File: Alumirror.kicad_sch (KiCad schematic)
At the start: 42 parts, among them J1 USB_C_Receptacle_USB2.0_16P_2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, J2 USB_C_Receptacle_USB2.0_16P_2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, J3 USB_C_Receptacle_USB2.0_16P_2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, J4 USB_C_Receptacle_USB2.0_16P_2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, SW10 BOOT, U1 CH552T, U2 CH552T, U3 USBLC6-2P6, U4 USBLC6-2P6, U5 USBLC6-2P6, U6 USBLC6-2P6

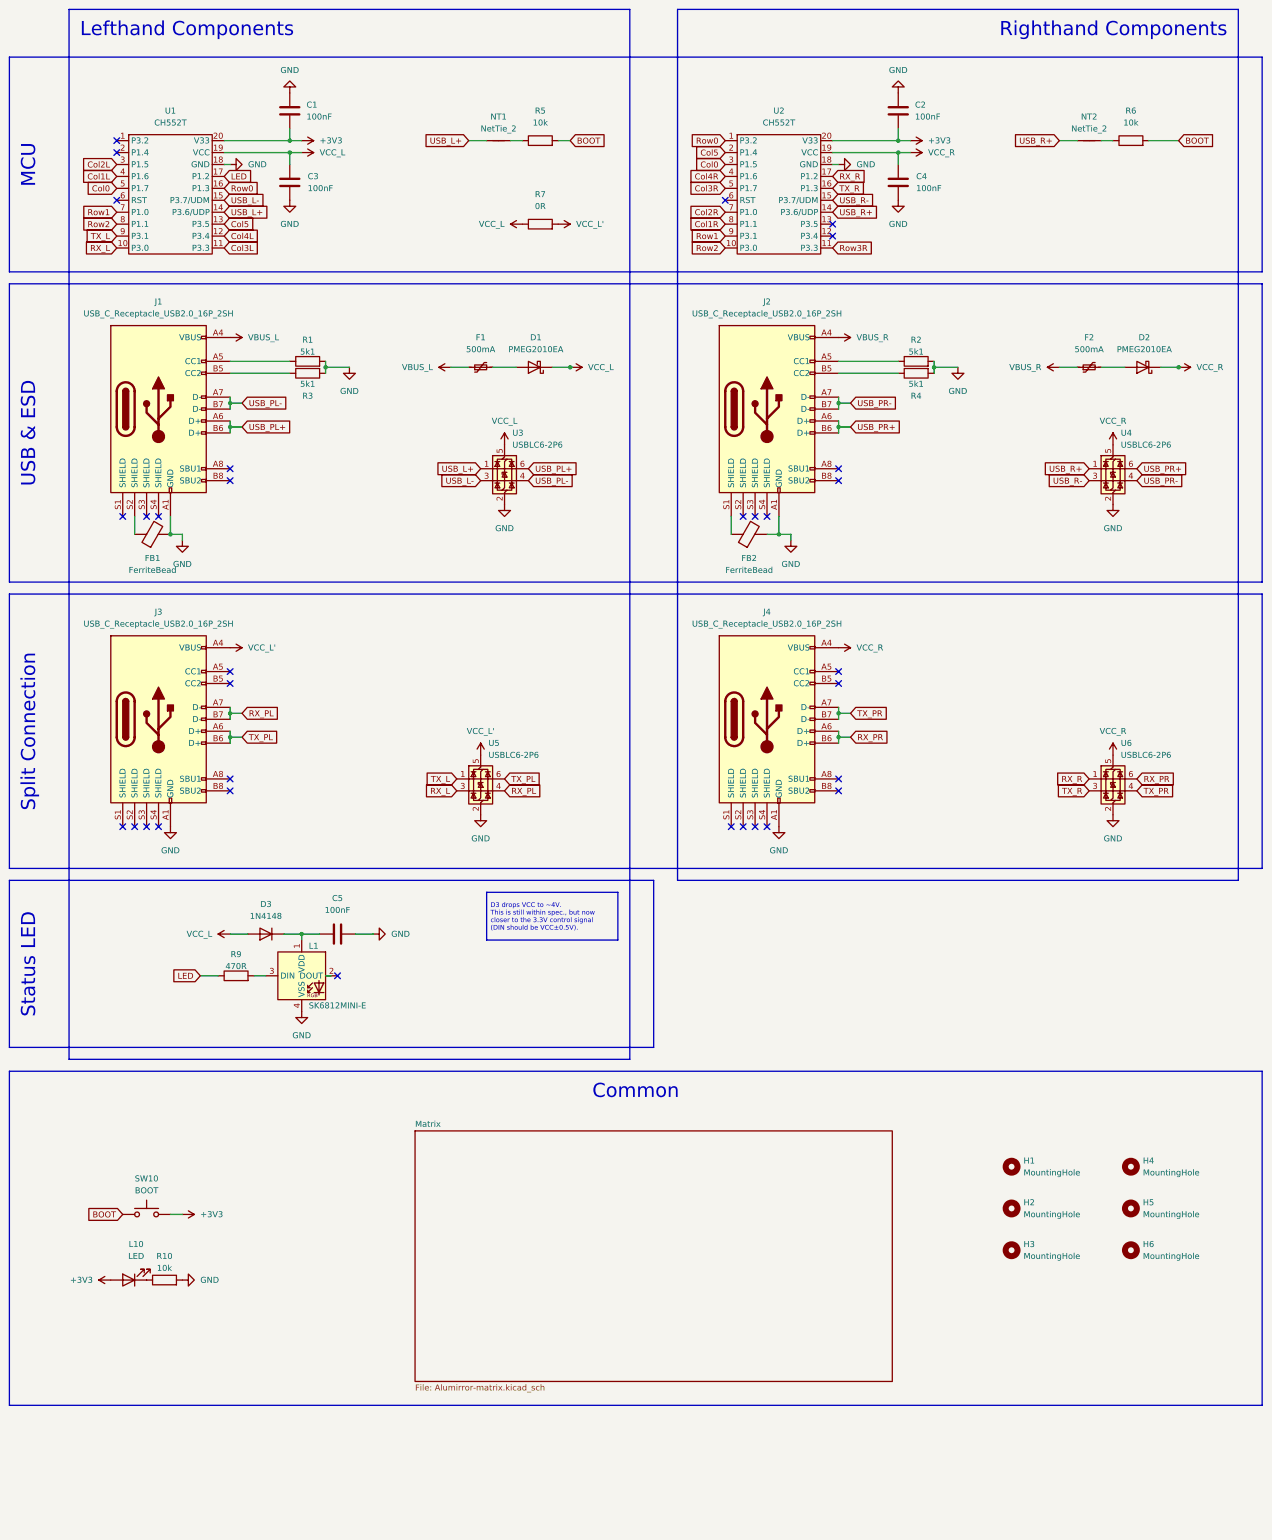
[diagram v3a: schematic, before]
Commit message: Renumber matrix switches and diodes
Columns and rows start from 1 rather than 0.
All components now follow the rules from the previous change, and we don’t had to mess around with the fake D-“oh” nonsense.
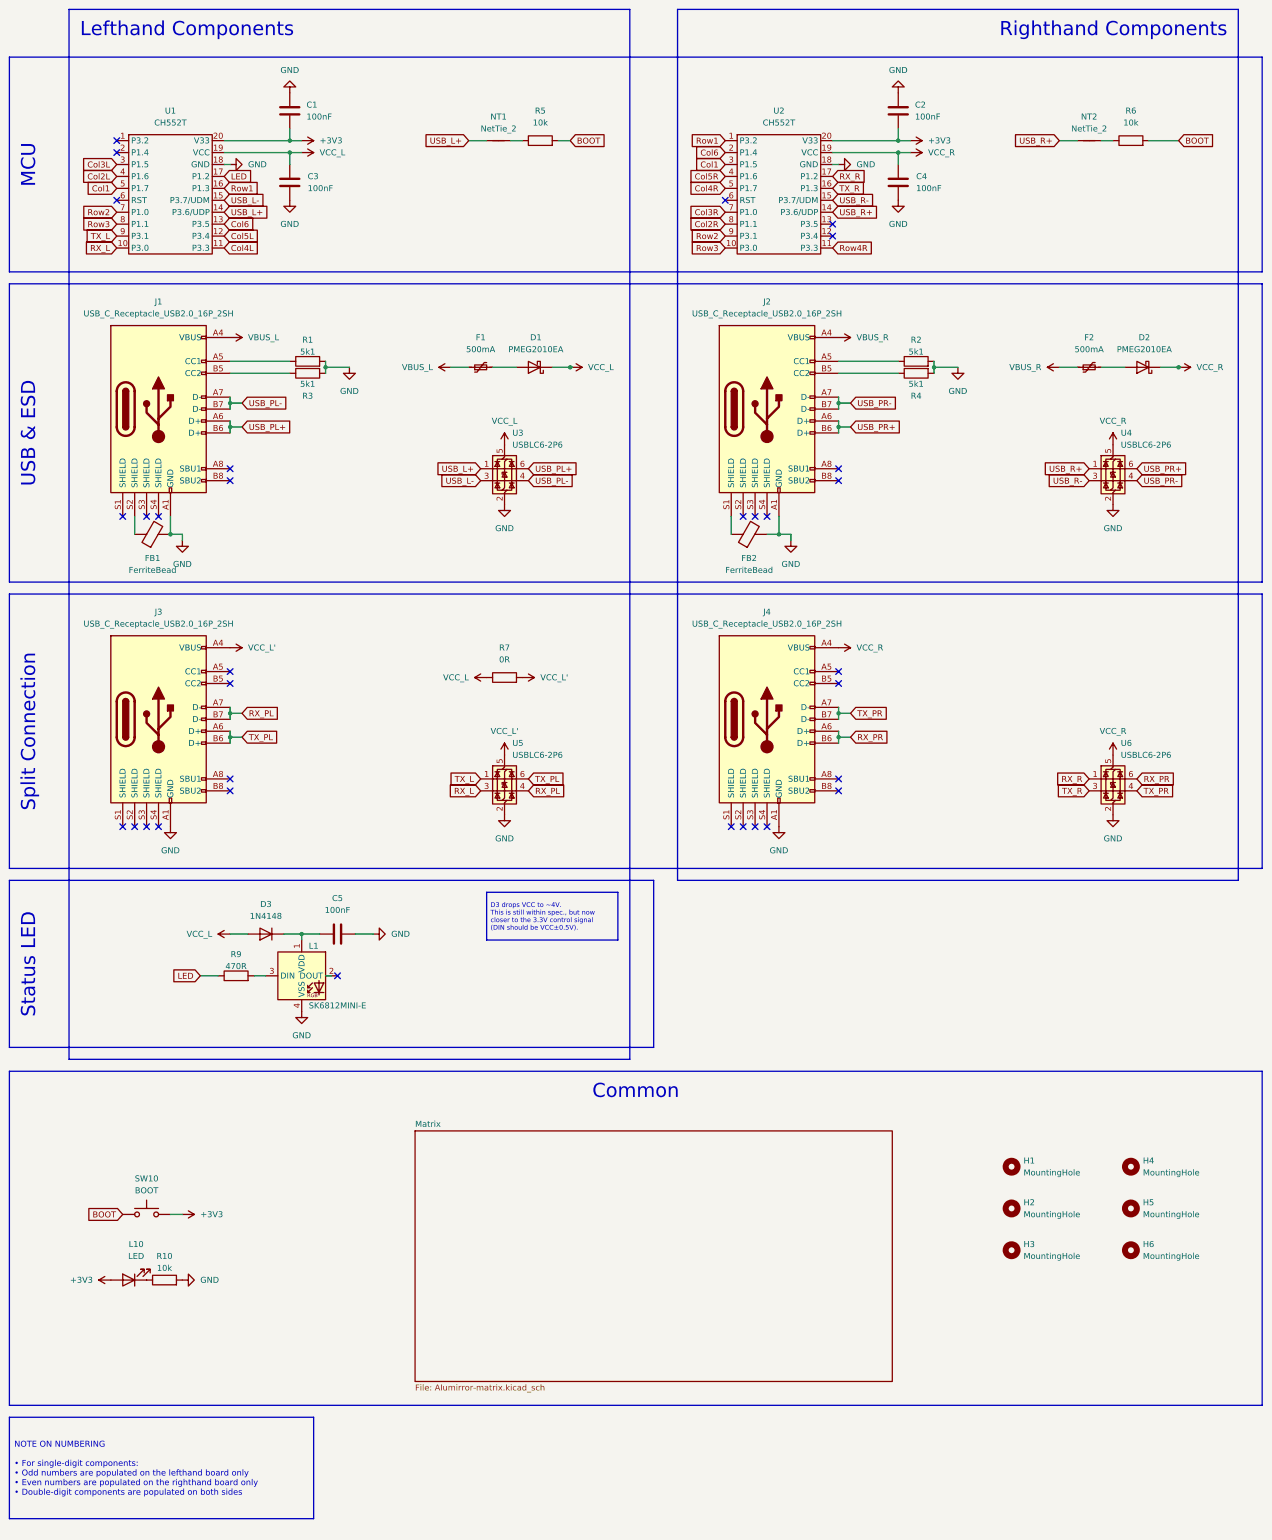
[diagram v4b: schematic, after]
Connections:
- net Col1L is gone; now on net Col2L: U1.4 (P1.6)
- net Col1R is gone; now on net Col2R: U2.8 (P1.1)
- net Row0 is gone; now on net Row1: U1.16 (P1.3), U2.1 (P3.2)
- net Col2L: no longer U1.3 (P1.5)
- net Col2R: no longer U2.7 (P1.0)
- net Col3L: now also U1.3 (P1.5); no longer U1.11 (P3.3)
- net Col3R: now also U2.7 (P1.0); no longer U2.5 (P1.7)
- net Col4L: now also U1.11 (P3.3); no longer U1.12 (P3.4)
- net Col4R: now also U2.5 (P1.7); no longer U2.4 (P1.6)
- net Row1: no longer U1.7 (P1.0), U2.9 (P3.1)
- net Row2: now also U1.7 (P1.0), U2.9 (P3.1); no longer U1.8 (P1.1), U2.10 (P3.0)
- net Col0 renamed Col1
- net Col5 renamed Col6
- net Row3R renamed Row4R
- new net Col5L: U1.12 (P3.4)
- new net Col5R: U2.4 (P1.6)
- new net Row3: U1.8 (P1.1), U2.10 (P3.0)
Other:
- moved on the sheet: R7, U5
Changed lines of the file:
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@@
 		)
 	)
+	(text_box "NOTE ON NUMBERING\n\n• For single-digit components:\n  • Odd numbers are populated on the lefthand board only\n  • Even numbers are populated on the righthand board only\n• Double-digit components are populated on both sides"
+		(exclude_from_sim no)
+		(at 15.24 314.96 0)
+		(size 64.77 21.59)
+		(stroke
+			(width 0)
+			(type default)
+		)
+		(fill
+			(type none)
+		)
+		(effects
+			(font
+				(size 1.27 1.27)
+			)
+			(justify left)
+		)
+	)
 	(text_box "Split Connection"
 		(exclude_from_sim no)
@@
 		)
 	)
-	(global_label "Col0"
+	(global_label "Col1"
 		(shape input)
 		(at 38.1 53.34 180)
@@
 	(global_label "TX_PL"
 		(shape input)
-		(at 120.65 179.07 0)
+		(at 125.73 179.07 0)
 		(fields_autoplaced yes)
 		(effects
@@
 		)
 		(property "Intersheetrefs" "${INTERSHEET_REFS}"
-			(at 129.078 179.07 0)
+			(at 134.158 179.07 0)
 			(effects
 				(font
@@
 		)
 	)
-	(global_label "Col4L"
+	(global_label "Col5L"
 		(shape input)
 		(at 60.96 63.5 0)
@@
 		)
 	)
-	(global_label "Row2"
+	(global_label "Row3"
 		(shape input)
 		(at 38.1 60.96 180)
@@
 		)
 	)
-	(global_label "Row1"
+	(global_label "Row2"
 		(shape input)
 		(at 38.1 58.42 180)
@@
 		)
 	)
-	(global_label "Col2L"
+	(global_label "Col3L"
 		(shape input)
 		(at 38.1 48.26 180)
@@
 		)
 	)
-	(global_label "Col1L"
+	(global_label "Col2L"
 		(shape input)
 		(at 38.1 50.8 180)
@@
 		)
 	)
-	(global_label "Col4R"
+	(global_label "Col5R"
 		(shape input)
 		(at 167.64 50.8 180)
@@
 		)
 	)
-	(global_label "Col3R"
+	(global_label "Col4R"
 		(shape input)
 		(at 167.64 53.34 180)
@@
 		)
 	)
-	(global_label "Col3L"
+	(global_label "Col4L"
 		(shape input)
 		(at 60.96 66.04 0)
@@
 		)
 	)
-	(global_label "Row3R"
+	(global_label "Row4R"
 		(shape input)
 		(at 190.5 66.04 0)
@@
 	(global_label "RX_L"
 		(shape input)
-		(at 110.49 181.61 180)
+		(at 115.57 181.61 180)
 		(fields_autoplaced yes)
 		(effects
@@
 		)
 		(property "Intersheetrefs" "${INTERSHEET_REFS}"
-			(at 103.0296 181.61 0)
+			(at 108.1096 181.61 0)
 			(effects
 				(font
@@
 		)
 	)
-	(global_label "Col1R"
+	(global_label "Col2R"
 		(shape input)
 		(at 167.64 60.96 180)
@@
 		)
 	)
-	(global_label "Row1"
+	(global_label "Row2"
 		(shape input)
 		(at 167.64 63.5 180)
@@
 	(global_label "TX_L"
 		(shape input)
-		(at 110.49 179.07 180)
+		(at 115.57 179.07 180)
 		(fields_autoplaced yes)
 		(effects
@@
 		)
 		(property "Intersheetrefs" "${INTERSHEET_REFS}"
-			(at 103.332 179.07 0)
+			(at 108.412 179.07 0)
 			(effects
 				(font
@@
 		)
 	)
-	(global_label "Col5"
+	(global_label "Col6"
 		(shape input)
 		(at 60.96 60.96 0)
@@
 		)
 	)
-	(global_label "Row2"
+	(global_label "Row3"
 		(shape input)
 		(at 167.64 66.04 180)
@@
 		)
 	)
-	(global_label "Col0"
+	(global_label "Col1"
 		(shape input)
 		(at 167.64 48.26 180)
@@
 		)
 	)
-	(global_label "Row0"
+	(global_label "Row1"
 		(shape input)
 		(at 60.96 53.34 0)
@@
 		)
 	)
-	(global_label "Row0"
+	(global_label "Row1"
 		(shape input)
 		(at 167.64 43.18 180)
@@
 		)
 	)
-	(global_label "Col5"
+	(global_label "Col6"
 		(shape input)
 		(at 167.64 45.72 180)
@@
 	(global_label "RX_PL"
 		(shape input)
-		(at 120.65 181.61 0)
+		(at 125.73 181.61 0)
 		(fields_autoplaced yes)
 		(effects
@@
 		)
 		(property "Intersheetrefs" "${INTERSHEET_REFS}"
-			(at 129.3804 181.61 0)
+			(at 134.4604 181.61 0)
 			(effects
 				(font
@@
 		)
 	)
-	(global_label "Col2R"
+	(global_label "Col3R"
 		(shape input)
 		(at 167.64 58.42 180)
@@
 	(symbol
 		(lib_id "power:VCC")
-		(at 115.57 173.99 0)
+		(at 120.65 173.99 0)
 		(unit 1)
 		(exclude_from_sim no)
@@
 		(fields_autoplaced yes)
 		(property "Reference" "#PWR02"
-			(at 115.57 177.8 0)
+			(at 120.65 177.8 0)
 			(effects
 				(font
@@
 		)
 		(property "Value" "VCC_L'"
-			(at 115.57 168.91 0)
+			(at 120.65 168.91 0)
 			(effects
 				(font
@@
 		)
 		(property "Footprint" ""
-			(at 115.57 173.99 0)
+			(at 120.65 173.99 0)
 			(effects
 				(font
@@
 		)
 		(property "Datasheet" ""
-			(at 115.57 173.99 0)
+			(at 120.65 173.99 0)
 			(effects
 				(font
@@
 		)
 		(property "Description" ""
-			(at 115.57 173.99 0)
+			(at 120.65 173.99 0)
 			(effects
 				(font
@@
 	(symbol
 		(lib_id "Power_Protection:USBLC6-2P6")
-		(at 115.57 179.07 0)
+		(at 120.65 179.07 0)
 		(unit 1)
 		(exclude_from_sim no)
@@
 		(fields_autoplaced yes)
 		(property "Reference" "U5"
-			(at 117.2211 171.45 0)
+			(at 122.3011 171.45 0)
 			(effects
 				(font
@@
 		)
 		(property "Value" "USBLC6-2P6"
-			(at 117.2211 173.99 0)
+			(at 122.3011 173.99 0)
 			(effects
 				(font
@@
 		)
 		(property "Footprint" "Project Library:SOT-666_Mod"
-			(at 116.586 185.801 0)
+			(at 121.666 185.801 0)
 			(effects
 				(font
@@
 		)
 		(property "Datasheet" "https://www.st.com/resource/en/datasheet/usblc6-2.pdf"
-			(at 116.586 187.706 0)
+			(at 121.666 187.706 0)
 			(effects
 				(font
@@
 		)
 		(property "Description" "Very low capacitance ESD protection diode, 2 data-line, SOT-666"
-			(at 115.57 179.07 0)
+			(at 120.65 179.07 0)
 			(effects
 				(font
@@
 	(symbol
 		(lib_id "power:GND")
-		(at 115.57 186.69 0)
+		(at 120.65 186.69 0)
 		(unit 1)
 		(exclude_from_sim no)
@@
 		(fields_autoplaced yes)
 		(property "Reference" "#PWR014"
-			(at 115.57 193.04 0)
+			(at 120.65 193.04 0)
 			(effects
 				(font
@@
 		)
 		(property "Value" "GND"
-			(at 115.57 191.77 0)
+			(at 120.65 191.77 0)
 			(effects
 				(font
@@
 		)
 		(property "Footprint" ""
-			(at 115.57 186.69 0)
+			(at 120.65 186.69 0)
 			(effects
 				(font
@@
 		)
 		(property "Datasheet" ""
-			(at 115.57 186.69 0)
+			(at 120.65 186.69 0)
 			(effects
 				(font
@@
 		)
 		(property "Description" "Power symbol creates a global label with name \"GND\" , ground"
-			(at 115.57 186.69 0)
+			(at 120.65 186.69 0)
 			(effects
 				(font
@@
 	(symbol
 		(lib_id "power:VCC")
-		(at 132.08 60.96 270)
+		(at 124.46 157.48 270)
 		(unit 1)
 		(exclude_from_sim no)
@@
 		(fields_autoplaced yes)
 		(property "Reference" "#PWR019"
-			(at 128.27 60.96 0)
+			(at 120.65 157.48 0)
 			(effects
 				(font
@@
 		)
 		(property "Value" "VCC_L'"
-			(at 135.89 60.9599 90)
+			(at 128.27 157.4799 90)
 			(effects
 				(font
@@
 		)
 		(property "Footprint" ""
-			(at 132.08 60.96 0)
+			(at 124.46 157.48 0)
 			(effects
 				(font
@@
 		)
 		(property "Datasheet" ""
-			(at 132.08 60.96 0)
+			(at 124.46 157.48 0)
 			(effects
 				(font
@@
 		)
 		(property "Description" ""
-			(at 132.08 60.96 0)
+			(at 124.46 157.48 0)
 			(effects
 				(font
@@
 	(symbol
 		(lib_id "Device:R")
-		(at 128.27 60.96 90)
+		(at 120.65 157.48 90)
 		(unit 1)
 		(exclude_from_sim no)
@@
 		(fields_autoplaced yes)
 		(property "Reference" "R7"
-			(at 128.27 54.61 90)
+			(at 120.65 151.13 90)
 			(effects
 				(font
@@
 		)
 		(property "Value" "0R"
-			(at 128.27 57.15 90)
+			(at 120.65 153.67 90)
 			(effects
 				(font
@@
 		)
 		(property "Footprint" "Resistor_SMD:R_2010_5025Metric"
-			(at 128.27 62.738 90)
+			(at 120.65 159.258 90)
 			(effects
 				(font
@@
 		)
 		(property "Datasheet" "~"
-			(at 128.27 60.96 0)
+			(at 120.65 157.48 0)
 			(effects
 				(font
@@
 		)
 		(property "Description" "Resistor"
-			(at 128.27 60.96 0)
+			(at 120.65 157.48 0)
 			(effects
 				(font
@@
 	(symbol
 		(lib_id "power:VCC")
-		(at 124.46 60.96 90)
+		(at 116.84 157.48 90)
 		(unit 1)
 		(exclude_from_sim no)
@@
 		(fields_autoplaced yes)
 		(property "Reference" "#PWR018"
-			(at 128.27 60.96 0)
+			(at 120.65 157.48 0)
 			(effects
 				(font
@@
 		)
 		(property "Value" "VCC_L"
-			(at 120.65 60.9599 90)
+			(at 113.03 157.4799 90)
 			(effects
 				(font
@@
 		)
 		(property "Footprint" ""
-			(at 124.46 60.96 0)
+			(at 116.84 157.48 0)
 			(effects
 				(font
@@
 		)
 		(property "Datasheet" ""
-			(at 124.46 60.96 0)
+			(at 116.84 157.48 0)
 			(effects
 				(font
@@
 		)
 		(property "Description" ""
-			(at 124.46 60.96 0)
+			(at 116.84 157.48 0)
 			(effects
 				(font
